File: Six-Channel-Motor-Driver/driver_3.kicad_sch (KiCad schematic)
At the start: 9 parts, among them J2 Screw_Terminal_01x02, Q1 Q_NMOS_GDS, Q2 Q_NMOS_GDS, Q3 Q_NMOS_GDS, Q4 Q_NMOS_GDS

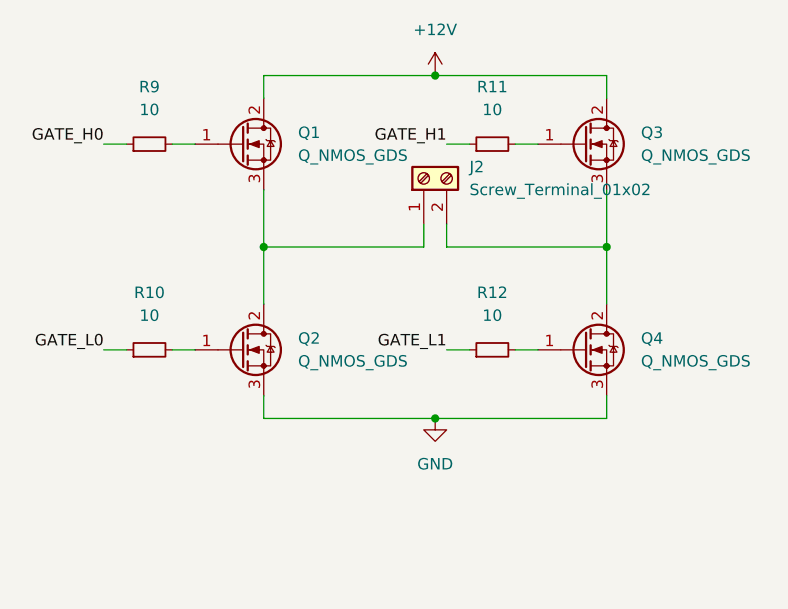
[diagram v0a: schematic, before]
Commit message: Added start of driver blocks
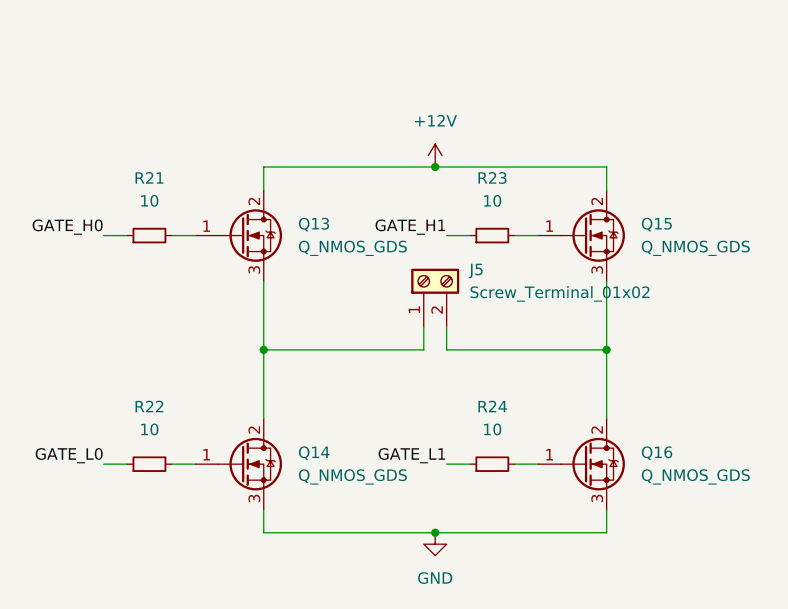
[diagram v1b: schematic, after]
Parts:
- removed J2: Screw_Terminal_01x02, Connector_Wire:SolderWire-2.5sqmm_1x02_P8.8mm_D2.4mm_OD4.4mm, symbol Connector:Screw_Terminal_01x02
- removed Q1, Q2, Q3, Q4: Q_NMOS_GDS, Package_TO_SOT_SMD:SOT-23, symbol Device:Q_NMOS_GDS
- removed R10, R11, R12, R9: 10, Resistor_SMD:R_0603_1608Metric, symbol Device:R_Small
- added J5: Screw_Terminal_01x02, Connector_Wire:SolderWire-2.5sqmm_1x02_P8.8mm_D2.4mm_OD4.4mm, symbol Connector:Screw_Terminal_01x02
- added Q13, Q14, Q15, Q16: Q_NMOS_GDS, Package_TO_SOT_SMD:SOT-23, symbol Device:Q_NMOS_GDS
- added R21, R22, R23, R24: 10, Resistor_SMD:R_0603_1608Metric, symbol Device:R_Small
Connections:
- net +12V: now also Q13.2 (D), Q15.2 (D)
- net GATE_H0: now also R21.1
- net GATE_H1: now also R23.1
- net GATE_L0: now also R22.1
- net GATE_L1: now also R24.1
- net GND: now also Q14.3 (S), Q16.3 (S)
- new net: Q16.1 (G), R24.2
- new net: Q15.1 (G), R23.2
- new net: J5.2 (Pin_2), Q15.3 (S), Q16.2 (D)
- new net: Q13.1 (G), R21.2
- new net: Q14.1 (G), R22.2
- new net: J5.1 (Pin_1), Q13.3 (S), Q14.2 (D)
